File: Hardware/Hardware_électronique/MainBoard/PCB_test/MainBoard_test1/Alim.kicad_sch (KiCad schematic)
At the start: 9 parts, among them Q1 PMOS

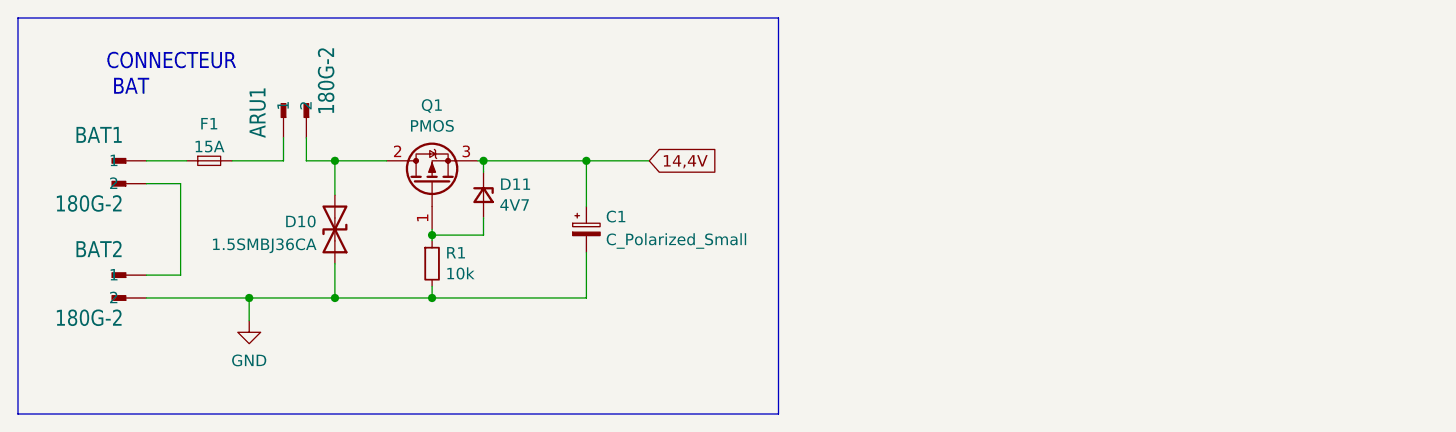
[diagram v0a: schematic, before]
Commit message: Adding motor board
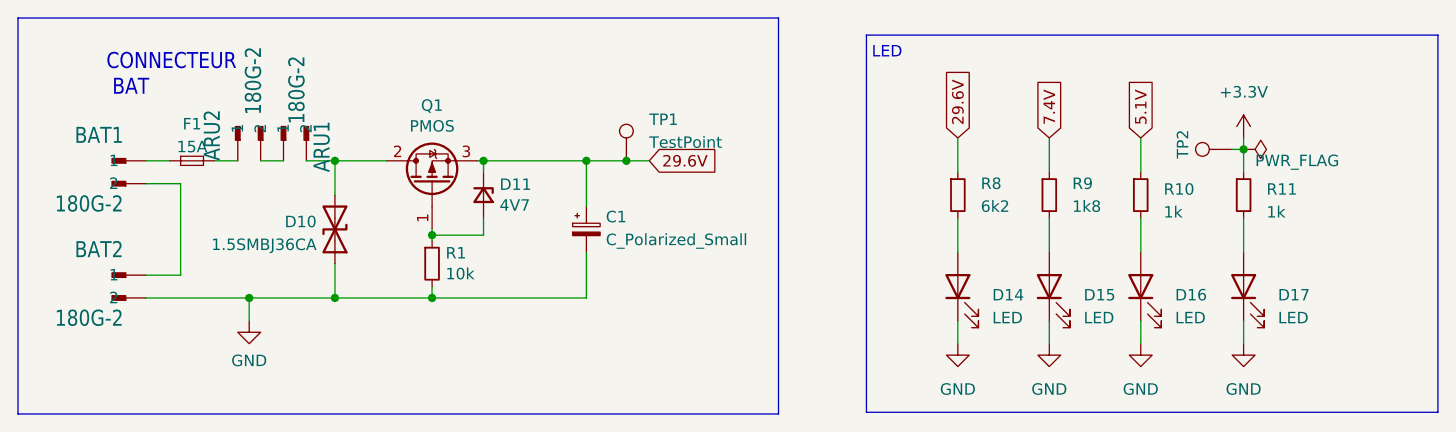
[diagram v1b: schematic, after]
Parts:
- added ARU2: 180G-2, MainBoard:180G-2, symbol schematic1-eagle-import:180G-2
- added D14, D15, D16, D17: LED, LED_SMD:LED_0603_1608Metric, symbol Device:LED
- added R10, R11: 1k, Resistor_SMD:R_0402_1005Metric, symbol Device:R_Small
- added R8: 6k2, Resistor_SMD:R_0402_1005Metric, symbol Device:R_Small
- added R9: 1k8, Resistor_SMD:R_0402_1005Metric, symbol Device:R_Small
- added TP1: TestPoint, symbol Connector:TestPoint
- added TP2: 3V3, Connector_Pin:Pin_D0.9mm_L10.0mm_W2.4mm_FlatFork, symbol Connector:TestPoint
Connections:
- net GND: now also D14.1 (K), D15.1 (K), D16.1 (K), D17.1 (K)
- net at F1.2: now also ARU2.1; no longer ARU1.1
- net 14,4V renamed 29.6V
- net 29.6V: now also R8.1, TP1.1
- new net: D14.2 (A), R8.2
- new net: D16.2 (A), R10.2
- new net: ARU1.1, ARU2.2
- new net: D15.2 (A), R9.2
- new net: D17.2 (A), R11.2
- new net +3.3V: R11.1, TP2.1
- new net 5.1V: R10.1
- new net 7.4V: R9.1
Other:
- note added: "LED"
- moved on the sheet: ARU1, F1
